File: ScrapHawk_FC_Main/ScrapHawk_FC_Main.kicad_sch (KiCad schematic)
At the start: 2 parts, among them U1 RP2040, U2 W25Q128JVS

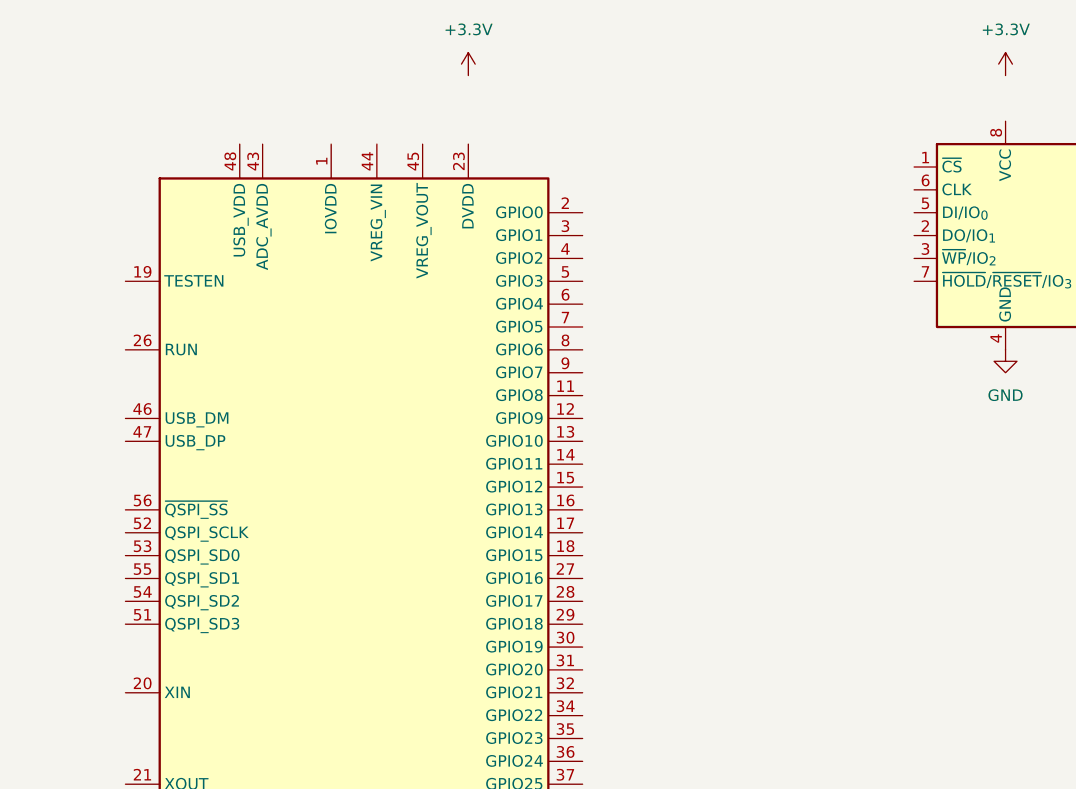
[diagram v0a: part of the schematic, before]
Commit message: add flash - rp2040 wire
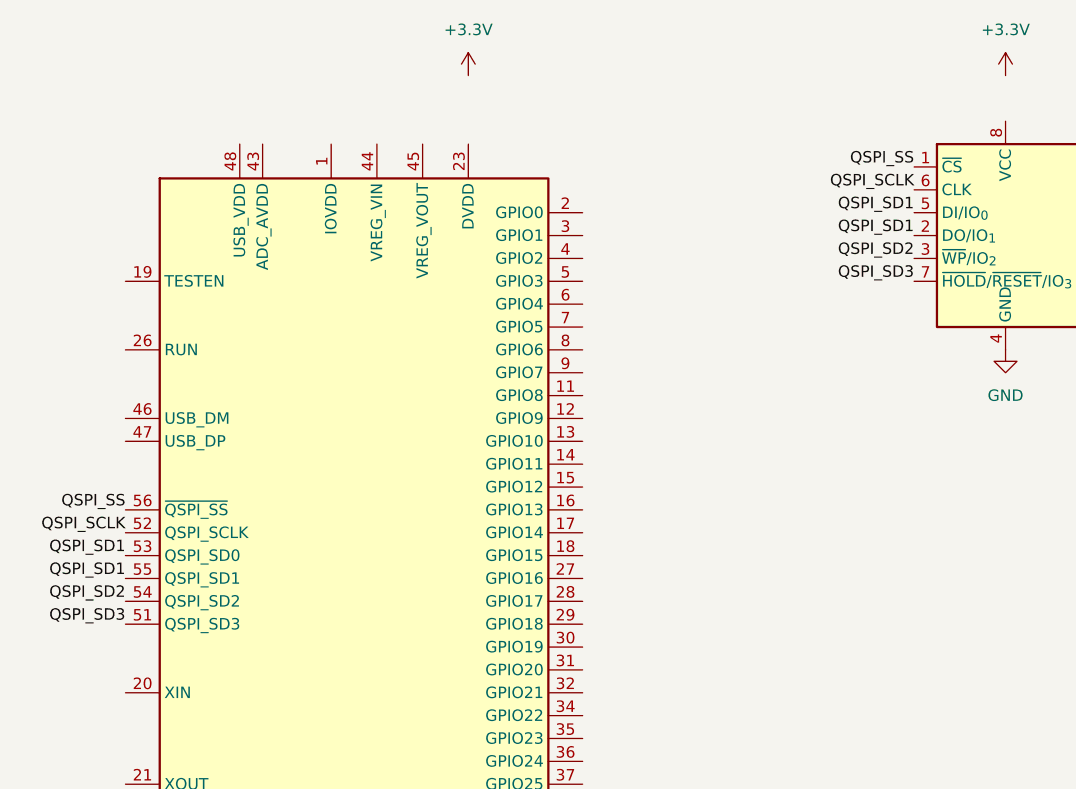
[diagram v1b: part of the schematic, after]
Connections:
- net QSPI_SS: now reaches U2.1 (~{CS})
- net QSPI_SS: now also U1.56 (~{QSPI_SS})
- net QSPI_SD1: now reaches U2.2 (DO/IO_{1})
- net QSPI_SD1: now also U1.53 (QSPI_SD0), U1.55 (QSPI_SD1), U2.5 (DI/IO_{0})
- net QSPI_SD2: now reaches U2.3 (~{WP}/IO_{2})
- net QSPI_SD2: now also U1.54 (QSPI_SD2)
- net QSPI_SCLK: now reaches U2.6 (CLK)
- net QSPI_SCLK: now also U1.52 (QSPI_SCLK)
- net QSPI_SD3: now reaches U2.7 (~{HOLD}/~{RESET}/IO_{3})
- net QSPI_SD3: now also U1.51 (QSPI_SD3)
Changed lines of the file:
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@@
 	(generator_version "10.0")
 	(paper "A3")
+	(label "QSPI_SS"
+		(at 147.32 43.18 180)
+		(effects
+			(font
+				(size 1.27 1.27)
+			)
+			(justify right bottom)
+		)
+	)
+	(label "QSPI_SD1"
+		(at 147.32 50.8 180)
+		(effects
+			(font
+				(size 1.27 1.27)
+			)
+			(justify right bottom)
+		)
+	)
+	(label "QSPI_SD2"
+		(at 147.32 53.34 180)
+		(effects
+			(font
+				(size 1.27 1.27)
+			)
+			(justify right bottom)
+		)
+	)
+	(label "QSPI_SD1"
+		(at 59.69 88.9 180)
+		(effects
+			(font
+				(size 1.27 1.27)
+			)
+			(justify right bottom)
+		)
+	)
+	(label "QSPI_SCLK"
+		(at 147.32 45.72 180)
+		(effects
+			(font
+				(size 1.27 1.27)
+			)
+			(justify right bottom)
+		)
+	)
+	(label "QSPI_SD2"
+		(at 59.69 91.44 180)
+		(effects
+			(font
+				(size 1.27 1.27)
+			)
+			(justify right bottom)
+		)
+	)
+	(label "QSPI_SD1"
+		(at 147.32 48.26 180)
+		(effects
+			(font
+				(size 1.27 1.27)
+			)
+			(justify right bottom)
+		)
+	)
+	(label "QSPI_SD3"
+		(at 59.69 93.98 180)
+		(effects
+			(font
+				(size 1.27 1.27)
+			)
+			(justify right bottom)
+		)
+	)
+	(label "QSPI_SS"
+		(at 59.69 81.28 180)
+		(effects
+			(font
+				(size 1.27 1.27)
+			)
+			(justify right bottom)
+		)
+	)
+	(label "QSPI_SD1"
+		(at 59.69 86.36 180)
+		(effects
+			(font
+				(size 1.27 1.27)
+			)
+			(justify right bottom)
+		)
+	)
+	(label "QSPI_SD3"
+		(at 147.32 55.88 180)
+		(effects
+			(font
+				(size 1.27 1.27)
+			)
+			(justify right bottom)
+		)
+	)
+	(label "QSPI_SCLK"
+		(at 59.69 83.82 180)
+		(effects
+			(font
+				(size 1.27 1.27)
+			)
+			(justify right bottom)
+		)
+	)
 	(symbol
 		(lib_id "Memory_Flash:W25Q128JVS")

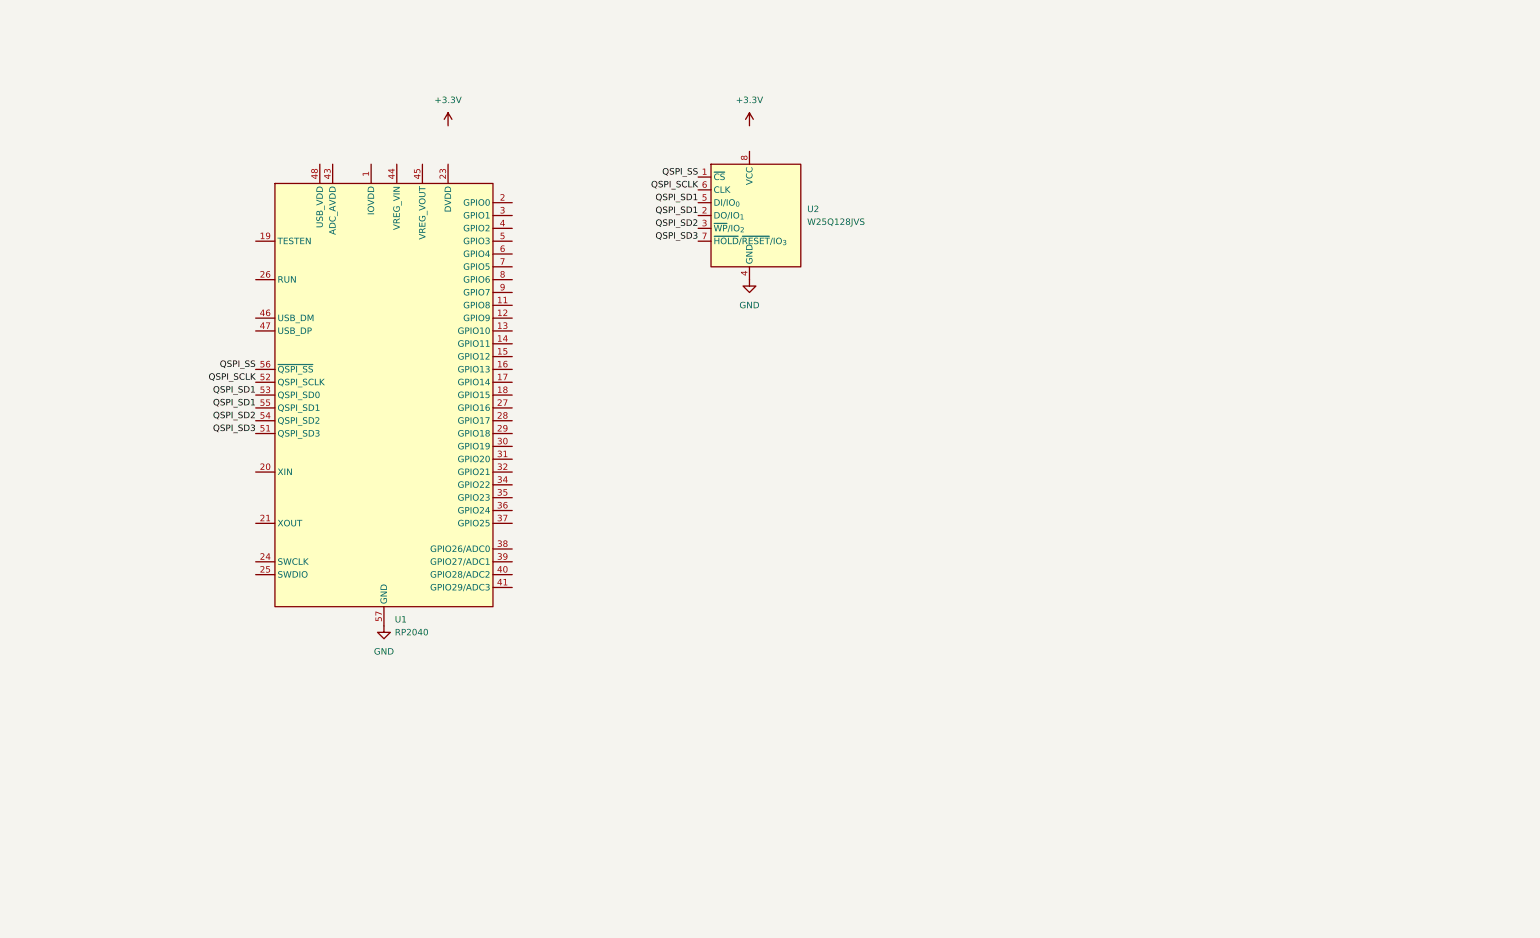
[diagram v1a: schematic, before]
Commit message: add step down + usb c connector wire
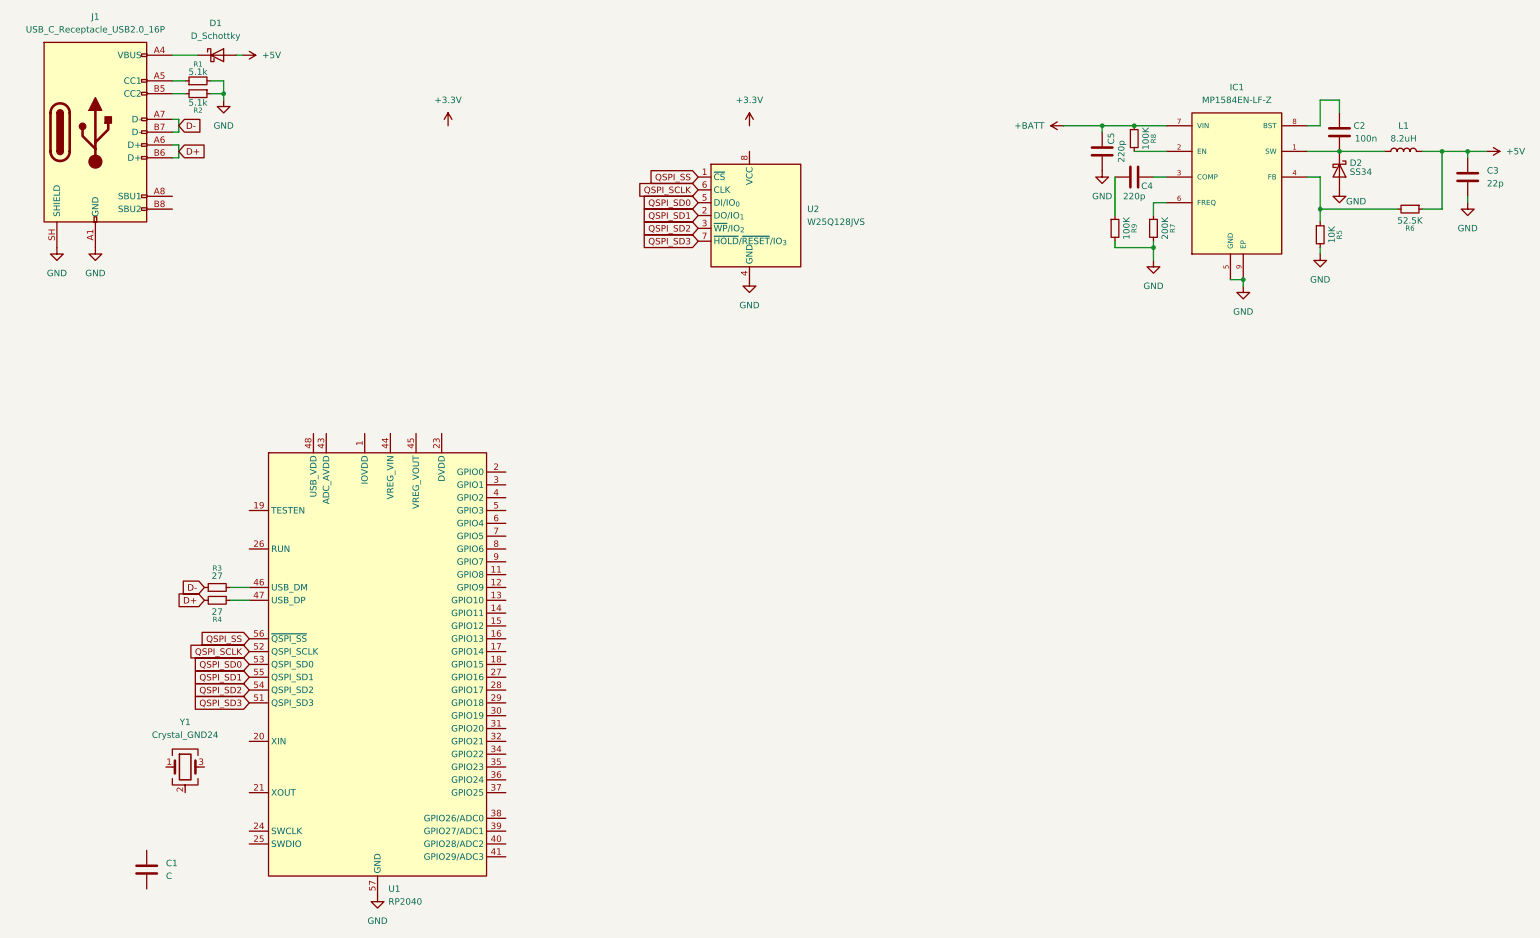
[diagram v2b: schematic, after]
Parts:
- added C1: C, symbol Device:C
- added C2: 100n, symbol Device:C
- added C3: 22p, symbol Device:C
- added C4, C5: 220p, symbol Device:C
- added D1: D_Schottky, symbol Device:D_Schottky
- added D2: SS34, symbol Device:D_Schottky
- added IC1: MP1584EN-LF-Z, MP1584EN-LF-Z:SOIC127P600X170-9N, symbol MP1584EN:MP1584EN-LF-Z
- added J1: USB_C_Receptacle_USB2.0_16P, symbol Connector:USB_C_Receptacle_USB2.0_16P
- added L1: 8.2uH, symbol Device:L
- added R1, R2: 5.1k, symbol Device:R_Small
- added R3, R4: 27, symbol Device:R_Small
- added R5: 10K, symbol Device:R_Small
- added R6: 52.5K, symbol Device:R_Small
- added R7: 200K, symbol Device:R_Small
- added R8, R9: 100K, symbol Device:R_Small
- added Y1: Crystal_GND24, symbol Device:Crystal_GND24
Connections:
- net GND: now also C3.2, C5.1, D2.2 (A), IC1.5 (GND), IC1.9 (EP), J1.A1 (GND), J1.A12 (GND), J1.B1 (GND), J1.B12 (GND), J1.SH (SHIELD), R1.2, R2.1, R5.2, R7.2, R9.2
- net QSPI_SD1: no longer U1.53 (QSPI_SD0), U2.5 (DI/IO_{0})
- net at U1.46 (USB_DM): now also R3.2
- net at U1.47 (USB_DP): now also R4.1
- new net: IC1.4 (FB), R5.1, R6.2
- new net: C4.1, R9.1
- new net: C2.2, D2.1 (K), IC1.1 (SW), L1.1
- new net: D1.1 (K), J1.A4 (VBUS), J1.A9 (VBUS), J1.B4 (VBUS), J1.B9 (VBUS)
- new net: IC1.2 (EN), R8.2
- new net: J1.A5 (CC1), R1.1
- new net: C4.2, IC1.3 (COMP)
- new net: IC1.6 (FREQ), R7.1
- new net: C2.1, IC1.8 (BST)
- new net: Y1.2 (G), Y1.4 (G)
- new net: J1.B5 (CC2), R2.2
- new net +5V: C3.1, D1.2 (A), L1.2, R6.1
- new net +BATT: C5.2, IC1.7 (VIN), R8.1
- new net D+: J1.A6 (D+), J1.B6 (D+), R4.2
- new net D-: J1.A7 (D-), J1.B7 (D-), R3.1
- new net QSPI_SD0: U1.53 (QSPI_SD0), U2.5 (DI/IO_{0})
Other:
- moved on the sheet: U1

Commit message: update gyro
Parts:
- removed C1: C, symbol Device:C
- removed C2: 100n, symbol Device:C
- removed C3: 22p, symbol Device:C
- removed C4, C5: 220p, symbol Device:C
- added C10, C13, C14, C20, C21, C22, C23, C25, C27, C28, C29, C7: 100n, Capacitor_SMD:C_0603_1608Metric, symbol Device:C_Small
- added C11, C12: 15p, Capacitor_SMD:C_0603_1608Metric, symbol Device:C_Small
- added C15, C16, C17, C18, C19: 22p, Capacitor_SMD:C_0603_1608Metric, symbol Device:C_Small
- added C24, C26: 1u, Capacitor_SMD:C_0603_1608Metric, symbol Device:C_Small
- added C8, C9: 220p, Capacitor_SMD:C_0603_1608Metric, symbol Device:C_Small
- added D3, D4: LED, Capacitor_SMD:C_0603_1608Metric, symbol Device:LED
- added R10: 100K, Resistor_SMD:R_0603_1608Metric, symbol Device:R_Small
- added R11, R12: 10K, Resistor_SMD:R_0603_1608Metric, symbol Device:R_Small
- added U3: AMS1117CD-3.3, Package_TO_SOT_SMD:SOT-223, symbol Regulator_Linear:AMS1117CD-3.3
- added U4: LSM6DS3TR, LSM6DS3TR:PQFN50P300X250X86-14N, symbol LSM6DS3TR:LSM6DS3TR
- D1: footprint (none) -> Diode_SMD:D_0805_2012Metric
- D2: footprint (none) -> Diode_SMD:D_SMC
- J1: footprint (none) -> Connector_USB:USB_C_Receptacle_G-Switch_GT-USB-7010ASV
- L1: footprint (none) -> Inductor_SMD:L_Chilisin_BMRA00050520
- R1, R2, R3, R4, R5, R6, R7, R8, R9: footprint (none) -> Resistor_SMD:R_0603_1608Metric
- Y1: value Crystal_GND24 -> 12M; footprint (none) -> Crystal:Crystal_SMD_SeikoEpson_TSX3225-4Pin_3.2x2.5mm
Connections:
- net +3.3V: now also U1.1 (IOVDD), U1.10 (IOVDD), U1.22 (IOVDD), U1.33 (IOVDD), U1.42 (IOVDD), U1.43 (ADC_AVDD), U1.44 (VREG_VIN), U1.48 (USB_VDD), U1.49 (IOVDD), U2.8 (VCC), C10.1, C13.2, C14.2, C16.1, C17.1, C20.2, C21.2, C22.2, C23.2, C24.2, C28.1, C29.2, R10.2, R11.1, R12.1, U3.2 (VO), U4.5 (VDDIO), U4.8 (VDD)
- net +5V: now also C15.1, C18.1, C19.1, U3.3 (VI)
- net +BATT: now also C8.1
- net GND: now also U1.19 (TESTEN), Y1.2 (G), Y1.4 (G), C10.2, C11.1, C12.1, C13.1, C14.1, C15.2, C16.2, C17.2, C18.2, C19.2, C20.1, C21.1, C22.1, C23.1, C24.1, C25.1, C26.1, C27.1, C28.2, C29.1, C8.2, U3.1 (GND), U4.6 (GND), U4.7 (GND__1)
- net QSPI_SS: now also R10.1
- net at R9.1: now also C9.1
- net at D2.1 (K), IC1.1 (SW), L1.1: now also C7.2
- net at IC1.3 (COMP): now also C9.2
- net at IC1.8 (BST): now also C7.1
- net at U1.20 (XIN): now also Y1.1, C11.2
- net at U1.21 (XOUT): now also Y1.3, C12.2
- net +1V1: now reaches U1.23 (DVDD), U1.50 (DVDD)
- net +1V1: now also U1.45 (VREG_VOUT), C25.2, C26.2, C27.2
- net MISO: now reaches U1.27 (GPIO16)
- net MISO: now also U4.1 (SDO/SA0)
- net CS: now reaches U1.28 (GPIO17)
- net CS: now also U4.12 (CS)
- net SCL: now reaches U1.29 (GPIO18)
- net SCL: now also U4.13 (SCL)
- net LED1: now reaches U1.3 (GPIO1)
- net LED1: now also D3.1 (K)
- net MOSI: now reaches U1.30 (GPIO19)
- net MOSI: now also U4.14 (SDA)
- net INT1: now reaches U1.31 (GPIO20)
- net INT1: now also U4.4 (INT1)
- net INT2: now reaches U1.32 (GPIO21)
- net INT2: now also U4.9 (INT2)
- net LED2: now reaches U1.4 (GPIO2)
- net LED2: now also D4.1 (K)
- new net: D4.2 (A), R12.2
- new net: D3.2 (A), R11.2
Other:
- moved on the sheet: Y1

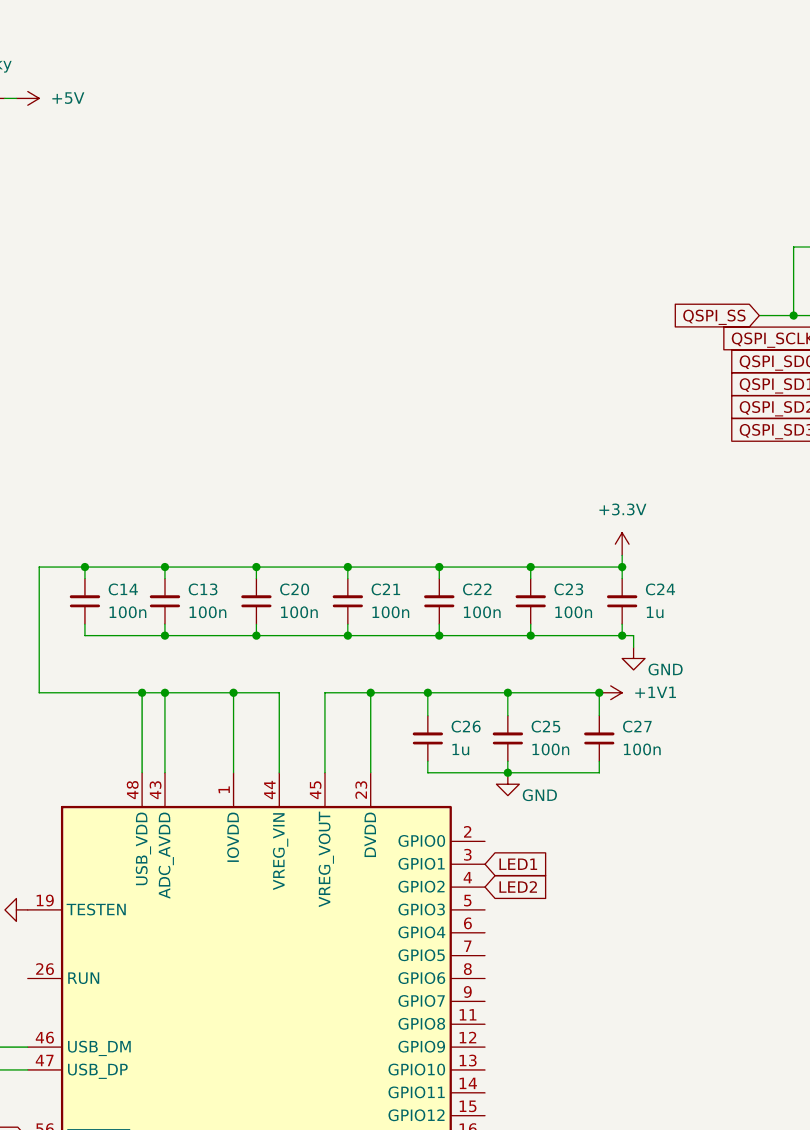
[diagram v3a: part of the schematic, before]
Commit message: wire pcb place components
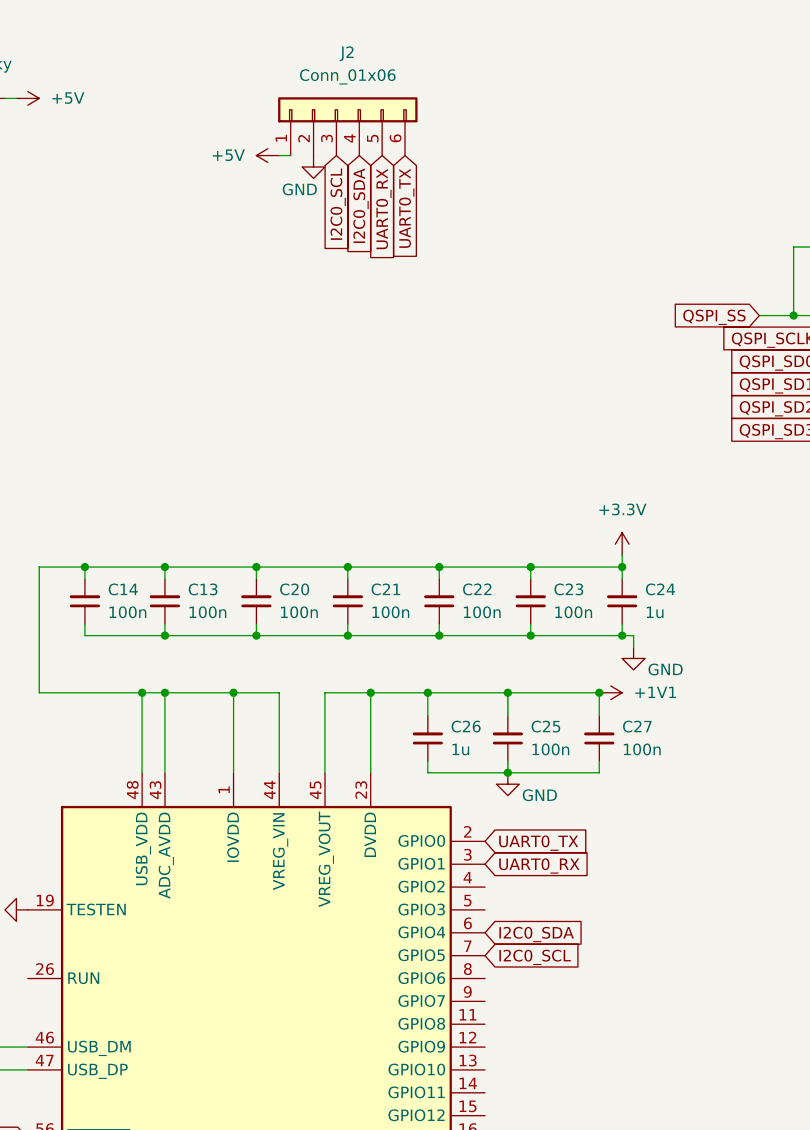
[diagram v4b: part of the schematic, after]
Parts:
- added J2: Conn_01x06, Connector_JST:JST_SH_BM06B-SRSS-TB_1x06-1MP_P1.00mm_Vertical, symbol Connector_Generic:Conn_01x06
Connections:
- net +5V: now also J2.1 (Pin_1)
- net GND: now also J2.2 (Pin_2)
- net LED1: no longer U1.3 (GPIO1)
- net LED2: no longer U1.4 (GPIO2)
- net UART0_TX: now reaches U1.2 (GPIO0)
- net UART0_TX: now also J2.6 (Pin_6)
- net I2C0_SDA: now reaches U1.6 (GPIO4)
- net I2C0_SDA: now also J2.4 (Pin_4)
- net I2C0_SCL: now reaches U1.7 (GPIO5)
- net I2C0_SCL: now also J2.3 (Pin_3)
- new net UART0_RX: J2.5 (Pin_5), U1.3 (GPIO1)

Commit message: finish pcb wiring
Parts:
- added J3: Conn_01x06, Connector_JST:JST_SH_BM06B-SRSS-TB_1x06-1MP_P1.00mm_Vertical, symbol Connector_Generic:Conn_01x06
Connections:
- net +BATT: now also J3.1 (Pin_1)
- net GND: now also J3.2 (Pin_2)
- net LED1: now also U1.15 (GPIO12)
- net LED2: now also U1.16 (GPIO13)
- net MOTOR1: now reaches U1.11 (GPIO8)
- net MOTOR1: now also J3.3 (Pin_3)
- net MOTOR2: now reaches U1.12 (GPIO9)
- net MOTOR2: now also J3.4 (Pin_4)
- net MOTOR3: now reaches U1.13 (GPIO10)
- net MOTOR3: now also J3.5 (Pin_5)
- net MOTOR4: now reaches U1.14 (GPIO11)
- net MOTOR4: now also J3.6 (Pin_6)
